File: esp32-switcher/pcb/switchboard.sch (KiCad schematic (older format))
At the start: 16 parts, among them J1 Conn_01x02, J10 Conn_01x02, J11 Conn_01x02, J12 Conn_01x02, J13 Conn_01x04, J14 Chain Out, J15 Chain In, J2 Conn_01x02, J3 Conn_01x02, J4 Conn_01x02, J5 Conn_01x02, J6 Conn_01x02, J7 Conn_01x02, J8 Conn_01x02, J9 Conn_01x02, U1 HiLetGo ESP-E32

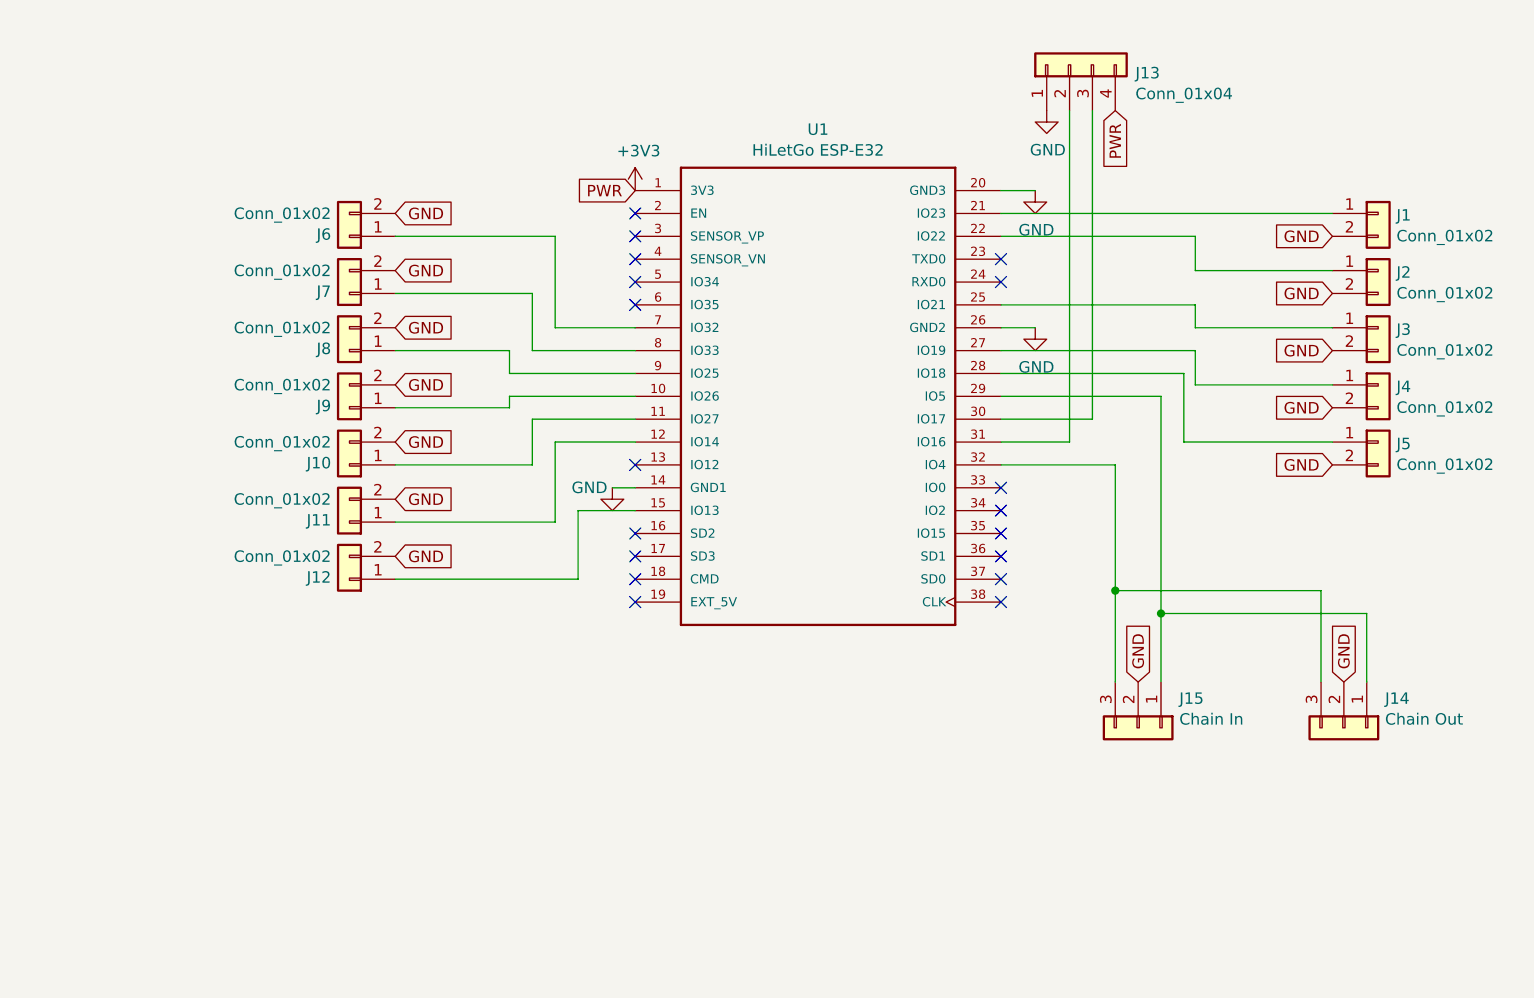
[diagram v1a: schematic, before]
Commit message: Add mounting holes and 2nd position for serial uart on switchboard
Also, "rescue" components on scart-input board. I gotta figure out what
that's about...
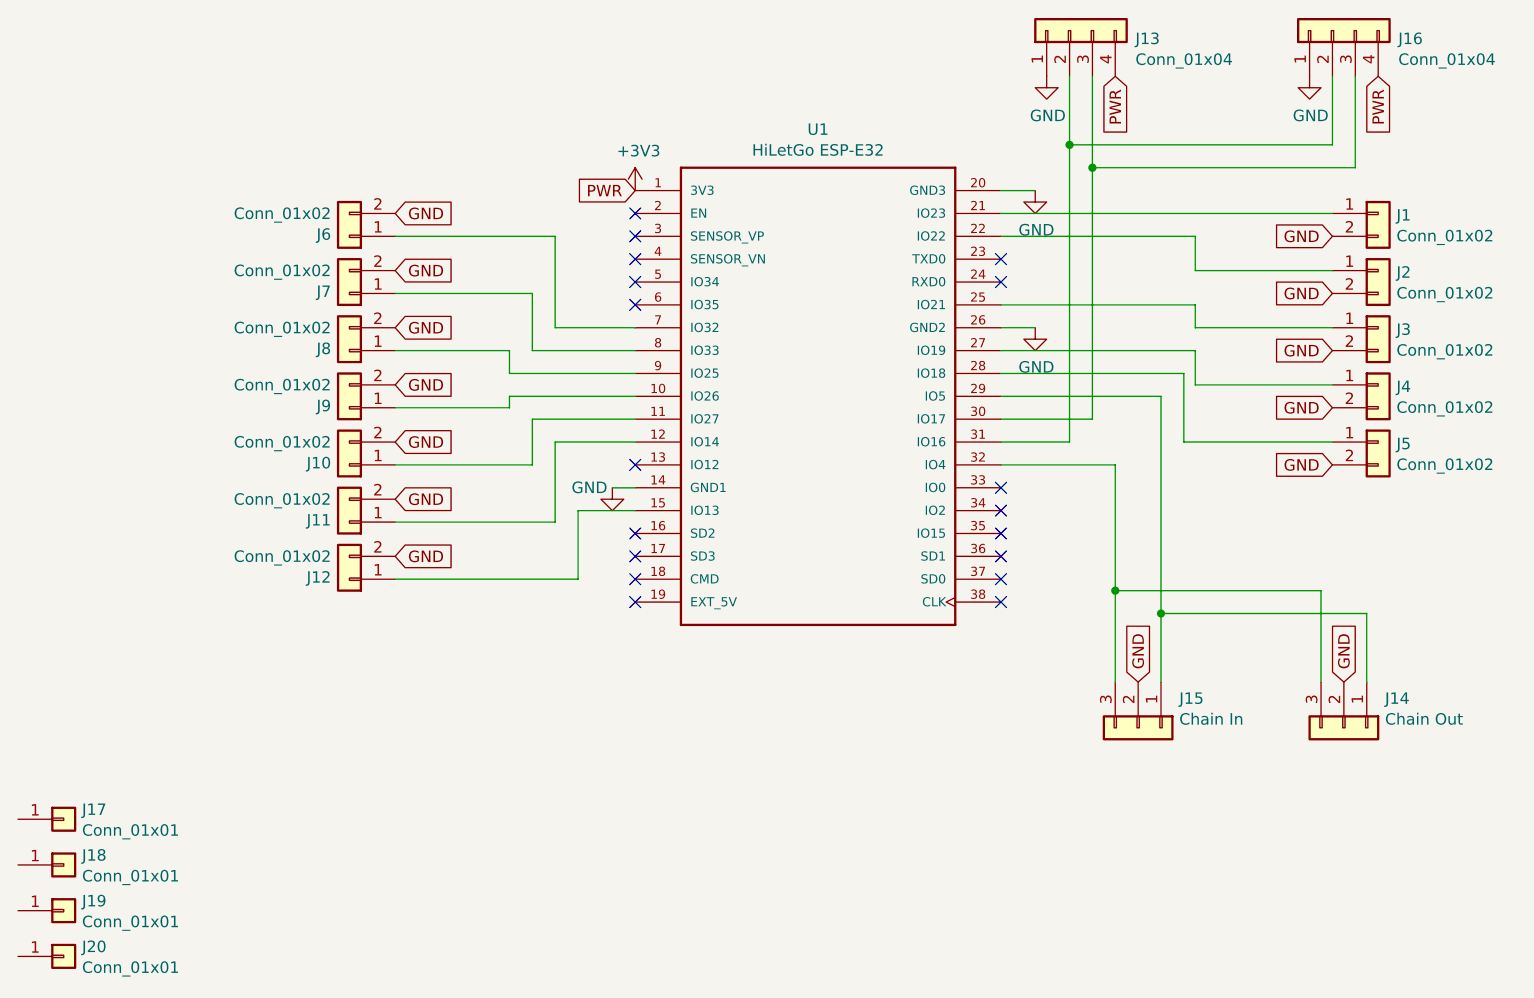
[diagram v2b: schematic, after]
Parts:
- added J16: Conn_01x04, Connector_PinSocket_2.54mm:PinSocket_1x04_P2.54mm_Vertical, symbol Connector_Generic:Conn_01x04
- added J17, J18, J19, J20: Conn_01x01, MountingHole:MountingHole_3.2mm_M3, symbol Connector_Generic:Conn_01x01
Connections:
- net +3V3: now also J16.4 (Pin_4)
- net GND: now also J16.1 (Pin_1)
- net at J13.3 (Pin_3), U1.30 (IO17): now also J16.3 (Pin_3)
- net at J13.2 (Pin_2), U1.31 (IO16): now also J16.2 (Pin_2)
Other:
- moved on the sheet: J13
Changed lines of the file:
@@
 Sheet 1 1
 Title "Extron ESP32 Switchboard"
-Date "2019-04-13"
-Rev "1.2"
+Date "2019-04-15"
+Rev "1.3"
 Comp "Rattboi (Bradon Kanyid)"
 Comment1 "https://github.com/rattboi/extron-scart-adapter"
@@
 L Connector_Generic:Conn_01x04 J13
 U 1 1 5CA19C8A
-P 6600 2250
-F 0 "J13" V 6564 1962 50  0000 R CNN
-F 1 "Conn_01x04" V 6473 1962 50  0000 R CNN
-F 2 "Connector_PinSocket_2.54mm:PinSocket_1x04_P2.54mm_Vertical" H 6600 2250 50  0001 C CNN
-F 3 "~" H 6600 2250 50  0001 C CNN
-	1    6600 2250
+P 6600 2100
+F 0 "J13" V 6564 1812 50  0000 R CNN
+F 1 "Conn_01x04" V 6473 1812 50  0000 R CNN
+F 2 "Connector_PinSocket_2.54mm:PinSocket_1x04_P2.54mm_Vertical" H 6600 2100 50  0001 C CNN
+F 3 "~" H 6600 2100 50  0001 C CNN
+	1    6600 2100
 	0    -1   -1   0
 $EndComp
@@
 	6300 3900 6600 3900
 Wire Wire Line
-	6700 3800 6700 2450
+	6700 3800 6700 2700
 Wire Wire Line
 	6300 3800 6700 3800
 Wire Wire Line
-	6600 3900 6600 2450
+	6600 3900 6600 2600
 $Comp
 L power:GND #PWR0101
 U 1 1 5CA2F4D0
-P 6500 2450
-F 0 "#PWR0101" H 6500 2200 50  0001 C CNN
-F 1 "GND" H 6505 2277 50  0000 C CNN
-F 2 "" H 6500 2450 50  0001 C CNN
-F 3 "" H 6500 2450 50  0001 C CNN
-	1    6500 2450
+P 6500 2300
+F 0 "#PWR0101" H 6500 2050 50  0001 C CNN
+F 1 "GND" H 6505 2127 50  0000 C CNN
+F 2 "" H 6500 2300 50  0001 C CNN
+F 3 "" H 6500 2300 50  0001 C CNN
+	1    6500 2300
 	1    0    0    -1
 $EndComp
@@
 Text GLabel 4700 2800 0    50   Input ~ 0
 PWR
-Text GLabel 6800 2450 3    50   Input ~ 0
+Text GLabel 6800 2300 3    50   Input ~ 0
 PWR
 $Comp
@@
 Wire Wire Line
 	4450 4200 4450 4500
+$Comp
+L Connector_Generic:Conn_01x04 J16
+U 1 1 5CB4BB5D
+P 7750 2100
+F 0 "J16" V 7714 1812 50  0000 R CNN
+F 1 "Conn_01x04" V 7623 1812 50  0000 R CNN
+F 2 "Connector_PinSocket_2.54mm:PinSocket_1x04_P2.54mm_Vertical" H 7750 2100 50  0001 C CNN
+F 3 "~" H 7750 2100 50  0001 C CNN
+	1    7750 2100
+	0    -1   -1   0
+$EndComp
+Wire Wire Line
+	6700 2700 7850 2700
+Wire Wire Line
+	7850 2700 7850 2300
+Wire Wire Line
+	6600 2600 7750 2600
+Wire Wire Line
+	7750 2600 7750 2300
+Connection ~ 6600 2600
+Wire Wire Line
+	6600 2600 6600 2300
+$Comp
+L power:GND #PWR0106
+U 1 1 5CB4EA20
+P 7650 2300
+F 0 "#PWR0106" H 7650 2050 50  0001 C CNN
+F 1 "GND" H 7655 2127 50  0000 C CNN
+F 2 "" H 7650 2300 50  0001 C CNN
+F 3 "" H 7650 2300 50  0001 C CNN
+	1    7650 2300
+	1    0    0    -1
+$EndComp
+Text GLabel 7950 2300 3    50   Input ~ 0
+PWR
+Connection ~ 6700 2700
+Wire Wire Line
+	6700 2300 6700 2700
+$Comp
+L Connector_Generic:Conn_01x01 J17
+U 1 1 5CB5F77A
+P 2200 5550
+F 0 "J17" H 2280 5592 50  0000 L CNN
+F 1 "Conn_01x01" H 2280 5501 50  0000 L CNN
+F 2 "MountingHole:MountingHole_3.2mm_M3" H 2200 5550 50  0001 C CNN
+F 3 "~" H 2200 5550 50  0001 C CNN
+	1    2200 5550
+	1    0    0    -1
+$EndComp
+$Comp
+L Connector_Generic:Conn_01x01 J18
+U 1 1 5CB5FF64
+P 2200 5750
+F 0 "J18" H 2280 5792 50  0000 L CNN
+F 1 "Conn_01x01" H 2280 5701 50  0000 L CNN
+F 2 "MountingHole:MountingHole_3.2mm_M3" H 2200 5750 50  0001 C CNN
+F 3 "~" H 2200 5750 50  0001 C CNN
+	1    2200 5750
+	1    0    0    -1
+$EndComp
+$Comp
+L Connector_Generic:Conn_01x01 J19
+U 1 1 5CB601A9
+P 2200 5950
+F 0 "J19" H 2280 5992 50  0000 L CNN
+F 1 "Conn_01x01" H 2280 5901 50  0000 L CNN
+F 2 "MountingHole:MountingHole_3.2mm_M3" H 2200 5950 50  0001 C CNN
+F 3 "~" H 2200 5950 50  0001 C CNN
+	1    2200 5950
+	1    0    0    -1
+$EndComp
+$Comp
+L Connector_Generic:Conn_01x01 J20
+U 1 1 5CB603FE
+P 2200 6150
+F 0 "J20" H 2280 6192 50  0000 L CNN
+F 1 "Conn_01x01" H 2280 6101 50  0000 L CNN
+F 2 "MountingHole:MountingHole_3.2mm_M3" H 2200 6150 50  0001 C CNN
+F 3 "~" H 2200 6150 50  0001 C CNN
+	1    2200 6150
+	1    0    0    -1
+$EndComp
 $EndSCHEMATC
